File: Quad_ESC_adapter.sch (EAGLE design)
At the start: 0 parts

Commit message: Final touches
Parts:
- added C1, C5, C6: 330uF, CAP, aluminin-capacitor-brick-UCM1H331MNL1GS:UCM1H331MNL1GS
- added H1, H2, H3, H4: 6-32-HOLE, Mounting Holes:6-32-HOLE
- added J1, J2, J3, J4: 284512-3, ThrusterConnector:284512-3
- added U$10: LUMENIER_QUAD-NO-CUT, Lumenier ESC:LUMENIER_QUAD-NO-CUT
- added U$2: BACKPLANE_ESC_ADAPTER_PWRESC, Backplane_ESC_adapter:BACKPLANE_ESC_ADAPTER_PWRESC
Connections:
- new net 12V: C1.+, C5.+, C6.+, U$10.VIN, U$2.12V
- new net ESC1_B: J1.3, U$10.M1P1
- new net ESC1_R: J1.1, U$10.M1P3
- new net ESC1_Y: J1.2, U$10.M1P2
- new net ESC2_B: J2.3, U$10.M2P1
- new net ESC2_R: J2.1, U$10.M2P3
- new net ESC2_Y: J2.2, U$10.M2P2
- new net ESC3_B: J3.1, U$10.M3P1
- new net ESC3_R: J3.3, U$10.M3P3
- new net ESC3_Y: J3.2, U$10.M3P2
- new net ESC4_B: J4.1, U$10.M4P1
- new net ESC4_R: J4.3, U$10.M4P3
- new net ESC4_Y: J4.2, U$10.M4P2
- new net GND: C1.-, C5.-, C6.-, U$10.GND, U$2.GND
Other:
- note added: "BACKPLANE CONNECTIONS"
- note added: "LUMENIER ESC"
- note added: "Move to backplane if these don't fit Or use through hole capacitor that comes with the Lumeniers"

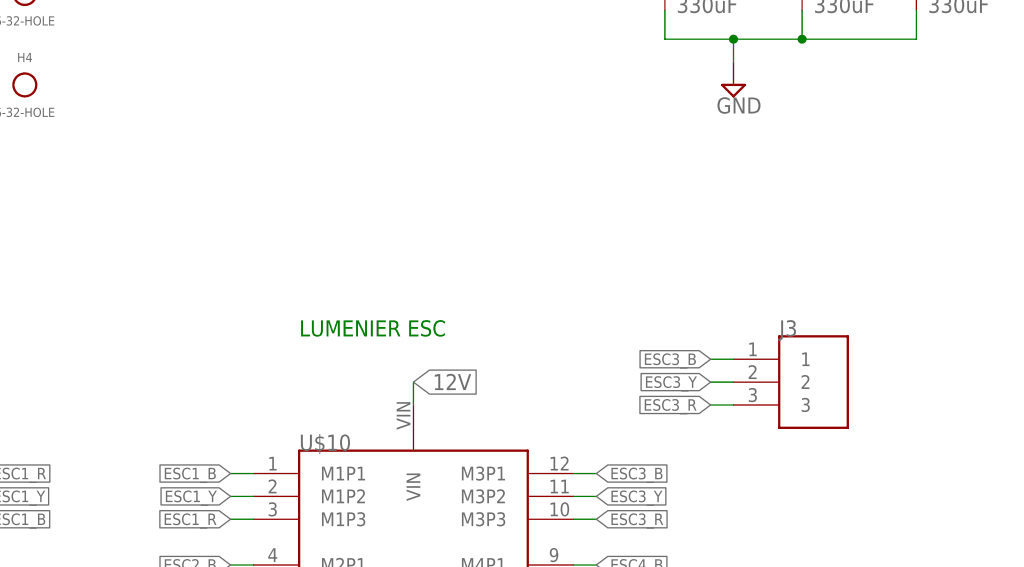
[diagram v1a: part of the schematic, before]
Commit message: Added status of chips
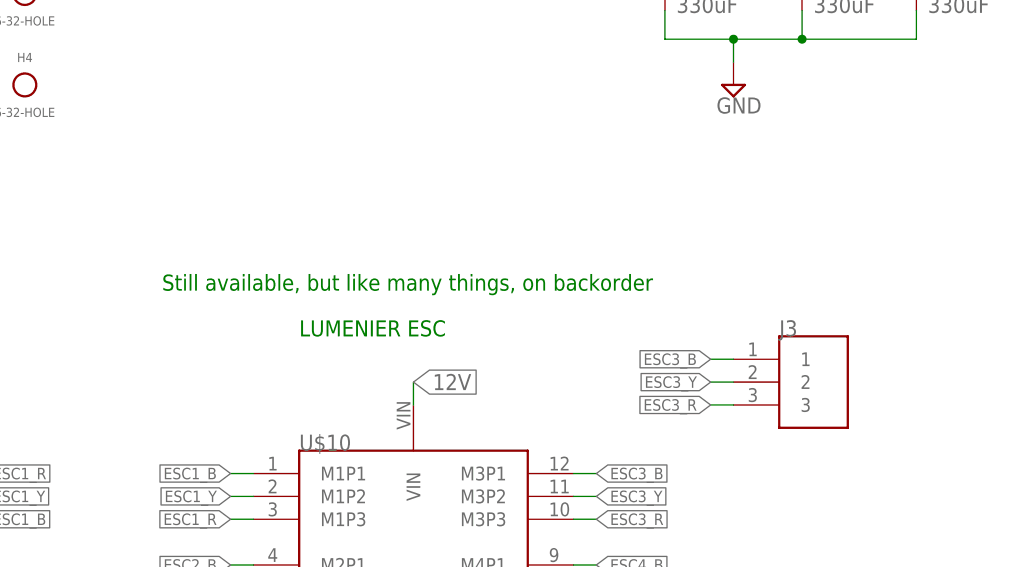
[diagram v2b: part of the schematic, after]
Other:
- note added: "Still available, but like many things, on backorder"
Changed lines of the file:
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@@
 <text x="149.86" y="114.3" size="1.778" layer="91">Move to backplane if these don't fit
 Or use through hole capacitor that comes with the Lumeniers</text>
+<text x="99.06" y="66.04" size="1.778" layer="91">Still available, but like many things, on backorder</text>
 </plain>
 <instances>

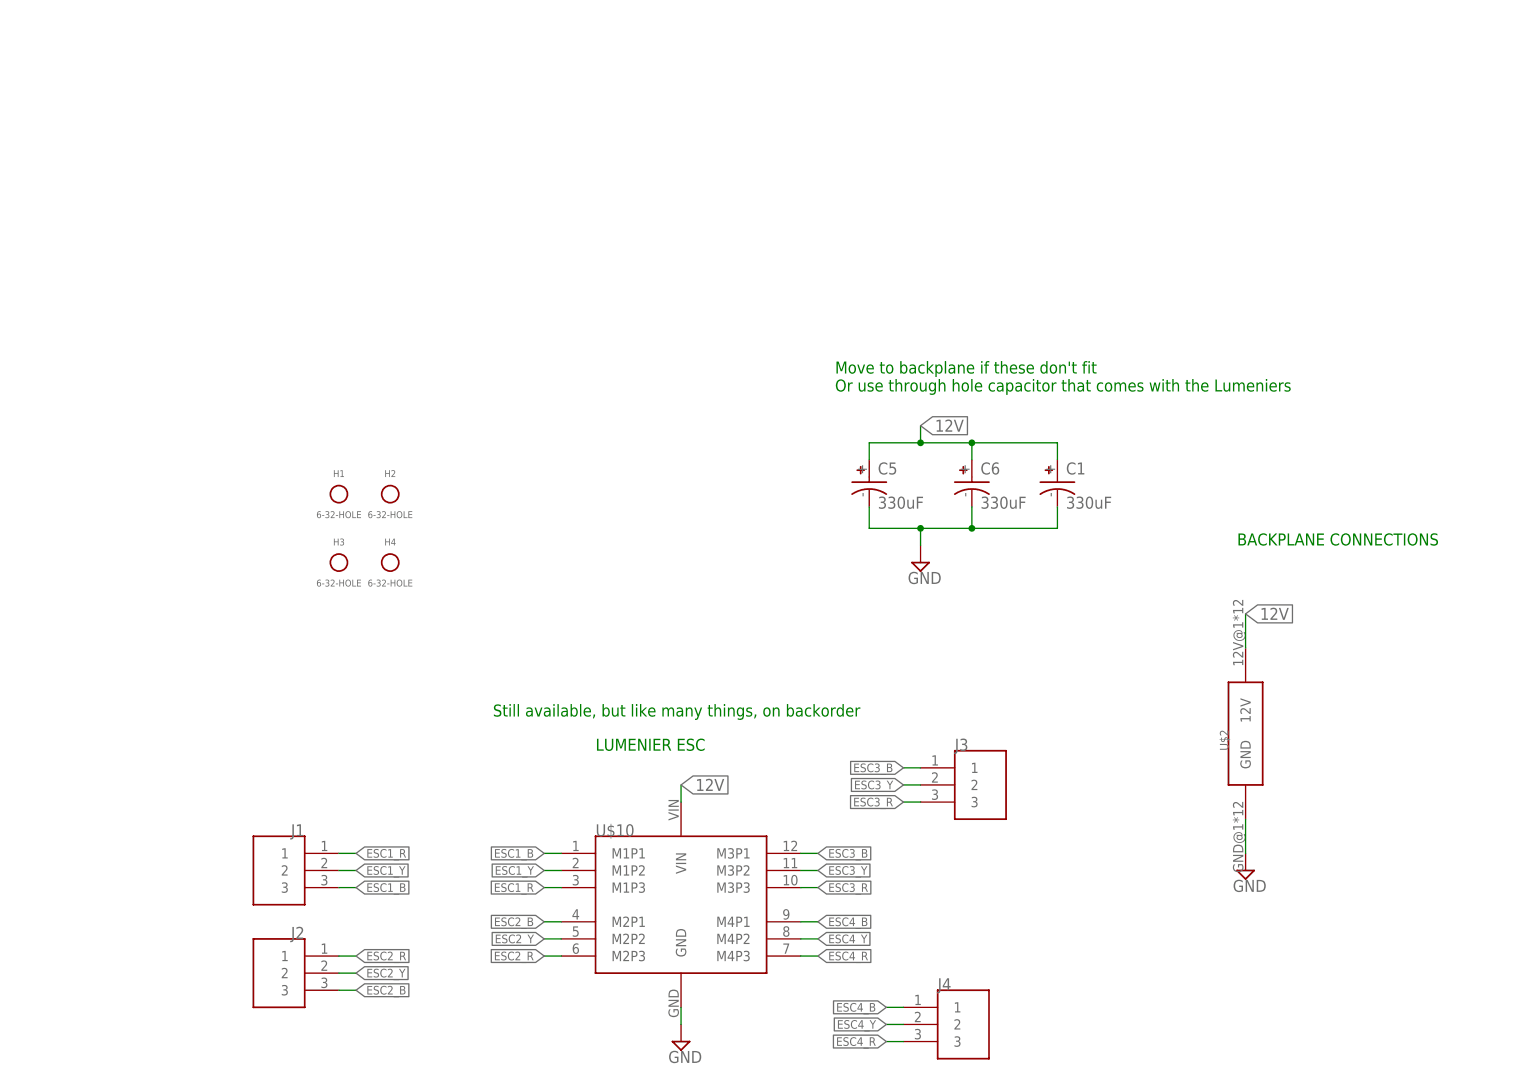
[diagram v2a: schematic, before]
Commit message: changed connectors
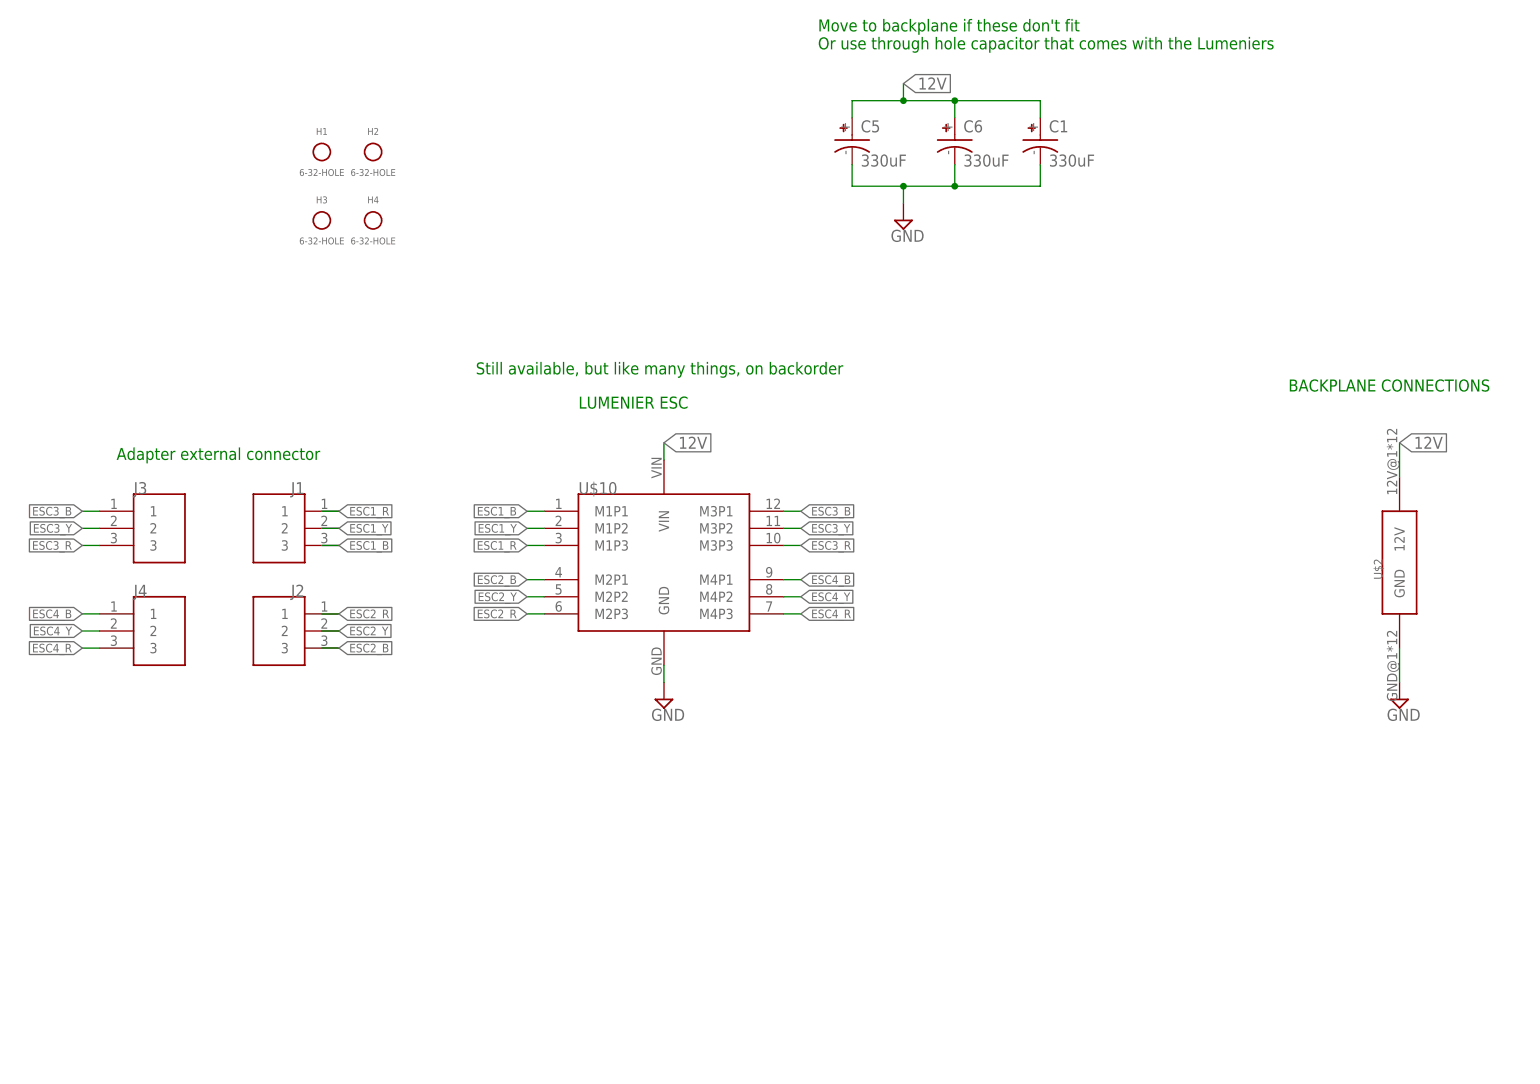
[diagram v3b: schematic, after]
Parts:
- J1, J2, J3, J4: value 284512-3 -> IBPD-SOCKET; device ThrusterConnector:284512-3 -> CONN, IPBD-03-S-K:IBPD-SOCKET
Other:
- note added: "Adapter external connector"
- moved on the sheet: C1, C5, C6, H1, H2, H3, H4, J1, J2, J3, J4, U$10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

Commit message: done bish
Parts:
- removed U$10: LUMENIER_QUAD-NO-CUT, Lumenier ESC:LUMENIER_QUAD-NO-CUT
- added U$1: LUMENIER_QUAD, AUX, Lumenier ESC:LUMENIER_QUAD
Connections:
- net 12V: now also U$1.VIN; no longer U$10.VIN
- net ESC1_B: now also U$1.M1P1; no longer U$10.M1P1
- net ESC1_R: now also U$1.M1P3; no longer U$10.M1P3
- net ESC1_Y: now also U$1.M1P2; no longer U$10.M1P2
- net ESC2_B: now also U$1.M2P1; no longer U$10.M2P1
- net ESC2_R: now also U$1.M2P3; no longer U$10.M2P3
- net ESC2_Y: now also U$1.M2P2; no longer U$10.M2P2
- net ESC3_B: now also U$1.M3P1; no longer U$10.M3P1
- net ESC3_R: now also U$1.M3P3; no longer U$10.M3P3
- net ESC3_Y: now also U$1.M3P2; no longer U$10.M3P2
- net ESC4_B: now also U$1.M4P1; no longer U$10.M4P1
- net ESC4_R: now also U$1.M4P3; no longer U$10.M4P3
- net ESC4_Y: now also U$1.M4P2; no longer U$10.M4P2
- net GND: now also U$1.GND; no longer U$10.GND

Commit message: check this
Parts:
- removed U$1: LUMENIER_QUAD, AUX, Lumenier ESC:LUMENIER_QUAD
- added U$10: LUMENIER_QUAD-NO-CUT, Lumenier ESC:LUMENIER_QUAD-NO-CUT
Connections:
- net 12V: now also U$10.VIN; no longer U$1.VIN
- net ESC1_B: now also U$10.M1P1; no longer U$1.M1P1
- net ESC1_R: now also U$10.M1P3; no longer U$1.M1P3
- net ESC1_Y: now also U$10.M1P2; no longer U$1.M1P2
- net ESC2_B: now also U$10.M2P1; no longer U$1.M2P1
- net ESC2_R: now also U$10.M2P3; no longer U$1.M2P3
- net ESC2_Y: now also U$10.M2P2; no longer U$1.M2P2
- net ESC3_B: now also U$10.M3P1; no longer U$1.M3P1
- net ESC3_R: now also U$10.M3P3; no longer U$1.M3P3
- net ESC3_Y: now also U$10.M3P2; no longer U$1.M3P2
- net ESC4_B: now also U$10.M4P1; no longer U$1.M4P1
- net ESC4_R: now also U$10.M4P3; no longer U$1.M4P3
- net ESC4_Y: now also U$10.M4P2; no longer U$1.M4P2
- net GND: now also U$10.GND; no longer U$1.GND
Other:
- note removed: "Adapter external connector"
- note removed: "Still available, but like many things, on backorder"
- moved on the sheet: C1, C5, C6, H1, H2, H3, H4, J1, J2, J3, J4, U$2

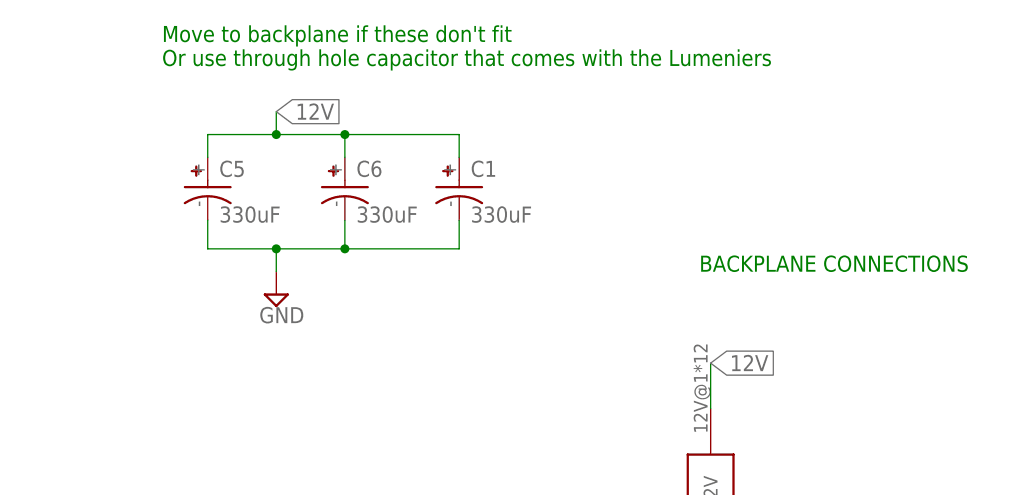
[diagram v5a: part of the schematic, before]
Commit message: added silkscreen, removed caps
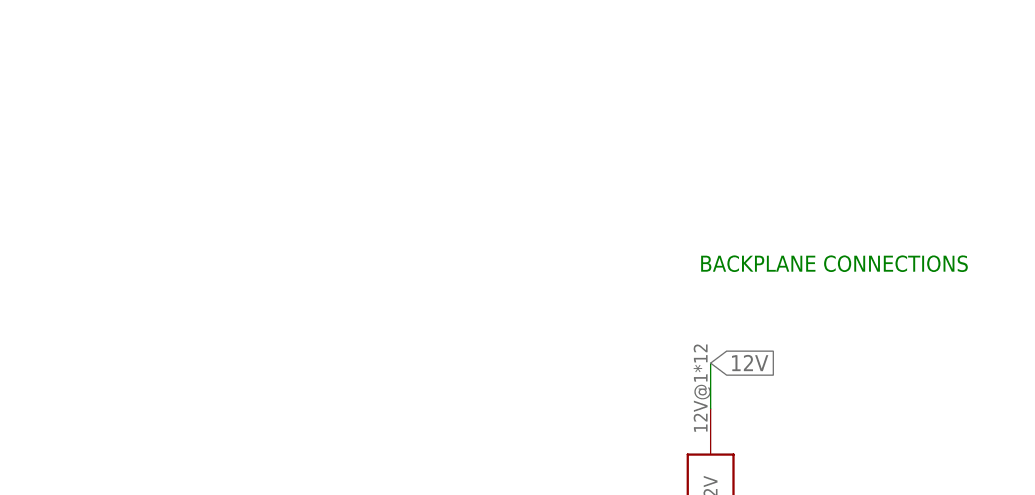
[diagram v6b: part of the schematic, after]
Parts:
- removed C1, C5, C6: 330uF, CAP, aluminin-capacitor-brick-UCM1H331MNL1GS:UCM1H331MNL1GS
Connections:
- net 12V: no longer C1.+, C5.+, C6.+
- net GND: no longer C1.-, C5.-, C6.-
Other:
- note removed: "Move to backplane if these don't fit Or use through hole capacitor that comes with the Lumeniers"
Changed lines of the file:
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@@
 <?xml version="1.0" encoding="utf-8"?>
 <!DOCTYPE eagle SYSTEM "eagle.dtd">
-<eagle version="9.6.2">
+<eagle version="9.5.0">
 <drawing>
 <settings>
@@
 <part name="U$10" library="Lumenier ESC" deviceset="LUMENIER_QUAD-NO-CUT" device="" package3d_urn="urn:adsk.eagle:package:24294694/3"/>
 <part name="SUPPLY5" library="supply2" library_urn="urn:adsk.eagle:library:372" deviceset="GND" device=""/>
-<part name="SUPPLY1" library="supply2" library_urn="urn:adsk.eagle:library:372" deviceset="GND" device=""/>
 <part name="SUPPLY4" library="supply2" library_urn="urn:adsk.eagle:library:372" deviceset="GND" device=""/>
 <part name="J1" library="CONN, IPBD-03-S-K" deviceset="IBPD-SOCKET" device=""/>
@@
 <part name="H4" library="Mounting Holes" deviceset="6-32-HOLE" device="" package3d_urn="urn:adsk.eagle:package:24384748/2"/>
 <part name="U$2" library="Backplane_ESC_adapter" deviceset="BACKPLANE_ESC_ADAPTER_PWR" device="ESC"/>
-<part name="C5" library="CAP, aluminin-capacitor-brick-UCM1H331MNL1GS" deviceset="UCM1H331MNL1GS" device="" package3d_urn="urn:adsk.eagle:package:24202090/2" value="330uF"/>
-<part name="C6" library="CAP, aluminin-capacitor-brick-UCM1H331MNL1GS" deviceset="UCM1H331MNL1GS" device="" package3d_urn="urn:adsk.eagle:package:24202090/2" value="330uF"/>
-<part name="C1" library="CAP, aluminin-capacitor-brick-UCM1H331MNL1GS" deviceset="UCM1H331MNL1GS" device="" package3d_urn="urn:adsk.eagle:package:24202090/2" value="330uF"/>
 </parts>
 <sheets>
@@
 <text x="209.55" y="91.44" size="1.778" layer="91">BACKPLANE CONNECTIONS</text>
 <text x="114.3" y="60.96" size="1.778" layer="91">LUMENIER ESC</text>
-<text x="149.86" y="114.3" size="1.778" layer="91">Move to backplane if these don't fit
-Or use through hole capacitor that comes with the Lumeniers</text>
 </plain>
 <instances>
@@
 <attribute name="VALUE" x="125.095" y="14.605" size="1.778" layer="96"/>
 </instance>
-<instance part="SUPPLY1" gate="GND" x="162.56" y="88.9" smashed="yes">
-<attribute name="VALUE" x="160.655" y="85.725" size="1.778" layer="96"/>
-</instance>
 <instance part="SUPPLY4" gate="GND" x="210.82" y="43.18" smashed="yes">
 <attribute name="VALUE" x="208.915" y="40.005" size="1.778" layer="96"/>
@@
 <instance part="U$2" gate="G$1" x="210.82" y="63.5" smashed="yes">
 <attribute name="NAME" x="208.28" y="60.96" size="1.27" layer="95" rot="R90"/>
-</instance>
-<instance part="C5" gate="G$1" x="154.94" y="101.6" smashed="yes">
-<attribute name="NAME" x="156.21" y="102.87" size="1.778" layer="95" align="center-left"/>
-<attribute name="VALUE" x="156.21" y="97.79" size="1.778" layer="95" align="center-left"/>
-</instance>
-<instance part="C6" gate="G$1" x="170.18" y="101.6" smashed="yes">
-<attribute name="NAME" x="171.45" y="102.87" size="1.778" layer="95" align="center-left"/>
-<attribute name="VALUE" x="171.45" y="97.79" size="1.778" layer="95" align="center-left"/>
-</instance>
-<instance part="C1" gate="G$1" x="182.88" y="101.6" smashed="yes">
-<attribute name="NAME" x="184.15" y="102.87" size="1.778" layer="95" align="center-left"/>
-<attribute name="VALUE" x="184.15" y="97.79" size="1.778" layer="95" align="center-left"/>
 </instance>
 </instances>
@@
 </segment>
 <segment>
-<wire x1="154.94" y1="93.98" x2="162.56" y2="93.98" width="0.1524" layer="91"/>
-<wire x1="162.56" y1="93.98" x2="170.18" y2="93.98" width="0.1524" layer="91"/>
-<wire x1="170.18" y1="93.98" x2="182.88" y2="93.98" width="0.1524" layer="91"/>
-<wire x1="182.88" y1="93.98" x2="182.88" y2="97.155" width="0.1524" layer="91"/>
-<wire x1="170.18" y1="97.155" x2="170.18" y2="93.98" width="0.1524" layer="91"/>
-<junction x="170.18" y="93.98"/>
-<wire x1="154.94" y1="97.155" x2="154.94" y2="93.98" width="0.1524" layer="91"/>
-<wire x1="162.56" y1="93.98" x2="162.56" y2="91.44" width="0.1524" layer="91"/>
-<junction x="162.56" y="93.98"/>
-<pinref part="SUPPLY1" gate="GND" pin="GND"/>
-<pinref part="C5" gate="G$1" pin="-"/>
-<pinref part="C6" gate="G$1" pin="-"/>
-<pinref part="C1" gate="G$1" pin="-"/>
-</segment>
-<segment>
 <pinref part="SUPPLY4" gate="GND" pin="GND"/>
 <wire x1="210.82" y1="45.72" x2="210.82" y2="50.8" width="0.1524" layer="91"/>
@@
 <wire x1="127" y1="53.34" x2="127" y2="55.88" width="0.1524" layer="91"/>
 <label x="127" y="55.88" size="1.778" layer="95" xref="yes"/>
-</segment>
-<segment>
-<wire x1="154.94" y1="106.68" x2="162.56" y2="106.68" width="0.1524" layer="91"/>
-<wire x1="162.56" y1="106.68" x2="170.18" y2="106.68" width="0.1524" layer="91"/>
-<wire x1="170.18" y1="106.68" x2="182.88" y2="106.68" width="0.1524" layer="91"/>
-<wire x1="182.88" y1="106.68" x2="182.88" y2="104.14" width="0.1524" layer="91"/>
-<wire x1="170.18" y1="104.14" x2="170.18" y2="106.68" width="0.1524" layer="91"/>
-<junction x="170.18" y="106.68"/>
-<wire x1="154.94" y1="104.14" x2="154.94" y2="106.68" width="0.1524" layer="91"/>
-<wire x1="162.56" y1="106.68" x2="162.56" y2="109.22" width="0.1524" layer="91"/>
-<junction x="162.56" y="106.68"/>
-<label x="162.56" y="109.22" size="1.778" layer="95" xref="yes"/>
-<pinref part="C5" gate="G$1" pin="+"/>
-<pinref part="C6" gate="G$1" pin="+"/>
-<pinref part="C1" gate="G$1" pin="+"/>
 </segment>
 <segment>
@@
 </drawing>
 <compatibility>
-<note version="6.3" minversion="6.2.2" severity="warning">
-Since Version 6.2.2 text objects can contain more than one line,
-which will not be processed correctly with this version.
-</note>
 <note version="8.2" severity="warning">
 Since Version 8.2, EAGLE supports online libraries. The ids
